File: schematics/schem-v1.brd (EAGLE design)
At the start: 33 x 54.3 mm, 13 parts, among them Q1 TIP120

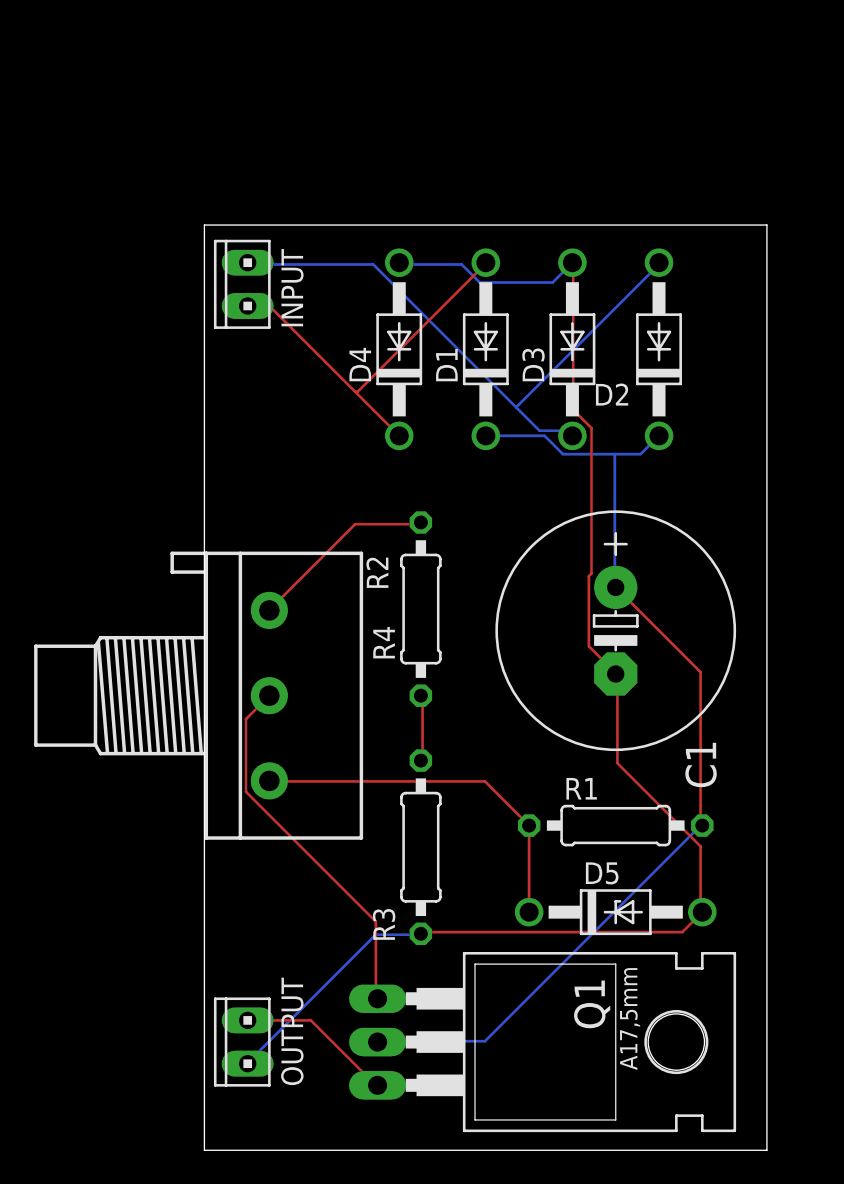
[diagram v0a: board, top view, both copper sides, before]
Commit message: second iteration: transformer adjustments
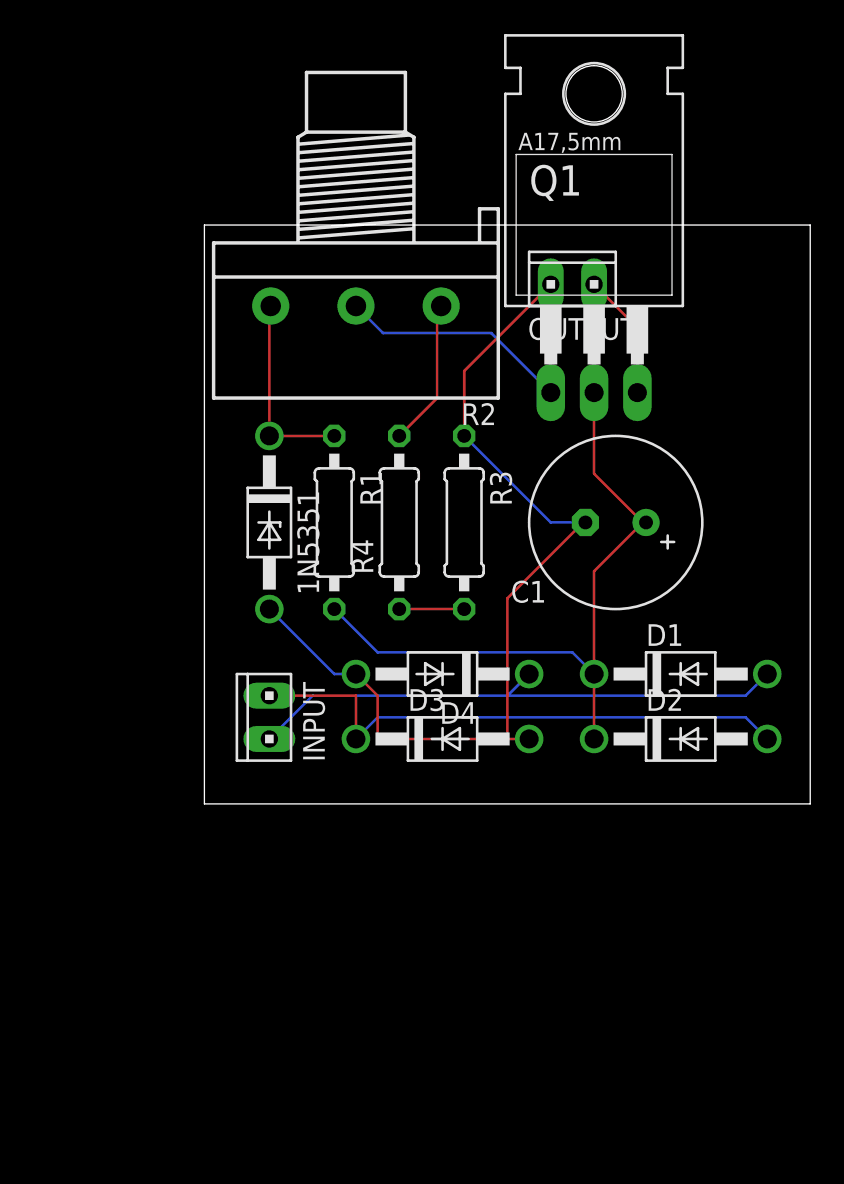
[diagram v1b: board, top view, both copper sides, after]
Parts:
- removed D5: (no value), diode:DO41Z10
- added 1N5351: (no value), diode:DO41Z10
- C1: value 1000uF -> 470uF; device rcl:E5-13 -> rcl:E3,5-10
- moved OUTPUT 48.4 mm to (21.6, 96.5), turned to 0 degrees
- moved Q1 44.9 mm to (22.9, 96.5), turned to 0 degrees
- moved INPUT 25.4 mm to (3.81, 71.1)
- moved R1 24.3 mm to (7.62, 82.5), turned to 270 degrees
- moved D3 24.1 mm to (14.0, 69.8), turned to 0 degrees
- moved R2 23.4 mm to (8.89, 95.2), turned to 180 degrees
- moved D2 22.9 mm to (27.9, 69.8), turned to 0 degrees
- moved D1 22.2 mm to (27.9, 73.7), turned to 0 degrees
- moved D4 19.2 mm to (14.0, 73.7), turned to 180 degrees
- moved R3 19.2 mm to (15.2, 82.5), turned to 270 degrees
- moved C1 6.35 mm to (24.1, 82.5), turned to 180 degrees
- moved R4 5.24 mm to (11.4, 82.5)
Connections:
- net GND: now also 1N5351.A; no longer D5.A
- net N$3: now also 1N5351.C; no longer D5.C
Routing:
- net GND: track 83.0 -> 54.8 mm
- net VCC: track 59.3 -> 39.7 mm
- net N$3: track 21.4 -> 11.5 mm
- net N$1: track 22.9 -> 32.6 mm
- net N$6: track 21.5 -> 13.5 mm
- net N$2: track 35.2 -> 32.8 mm
- net N$4: track 11.1 -> 8.78 mm
- net N$7: track 9.20 -> 7.40 mm
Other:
- board size 33 x 54.3 mm -> 35.5 x 34 mm
